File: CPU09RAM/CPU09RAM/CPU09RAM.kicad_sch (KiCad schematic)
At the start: 48 parts, among them J1 BUS, SW1 SW_DIP_x08, U1 74HC21, U10 AS6C4008-55PCN, U11 AS6C4008-55PCN, U12 74HC139, U13 74HC574, U14 74HC574, U15 74HC245, U16 74HC245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

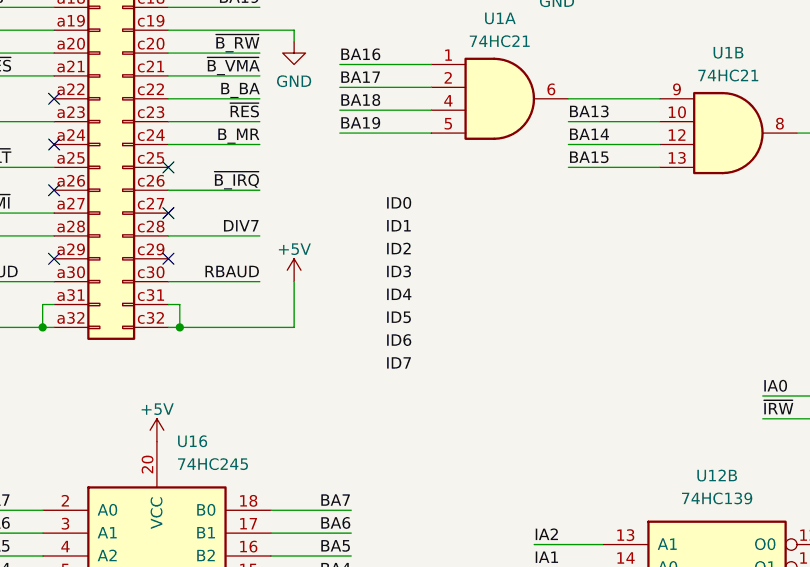
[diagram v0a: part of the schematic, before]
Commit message: 09NET added, 09FLP minor ch.
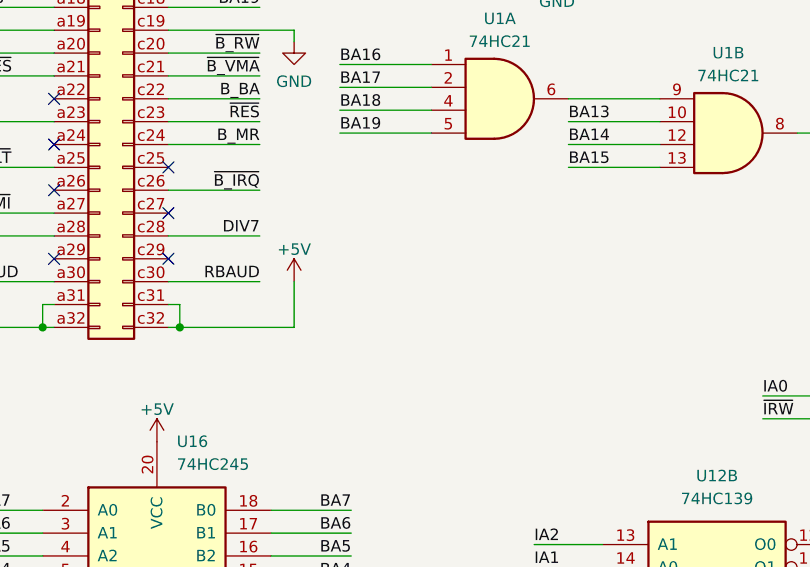
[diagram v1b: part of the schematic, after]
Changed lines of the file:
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@@
 		)
 	)
-	(label "ID2"
-		(at 67.31 92.71 0)
-		(effects
-			(font
-				(size 1.27 1.27)
-			)
-			(justify left bottom)
-		)
-	)
 	(label "LA8"
 		(at 113.03 173.99 180)
@@
 		)
 	)
-	(label "ID3"
-		(at 67.31 95.25 0)
-		(effects
-			(font
-				(size 1.27 1.27)
-			)
-			(justify left bottom)
-		)
-	)
 	(label "~{EXT}"
 		(at 53.34 29.21 180)
@@
 		)
 	)
-	(label "ID7"
-		(at 67.31 105.41 0)
-		(effects
-			(font
-				(size 1.27 1.27)
-			)
-			(justify left bottom)
-		)
-	)
 	(label "LA4"
 		(at 254 134.62 0)
@@
 		)
 	)
-	(label "ID1"
-		(at 67.31 90.17 0)
-		(effects
-			(font
-				(size 1.27 1.27)
-			)
-			(justify left bottom)
-		)
-	)
 	(label "IA3"
 		(at 254 39.37 0)
@@
 		)
 	)
-	(label "ID4"
-		(at 67.31 97.79 0)
-		(effects
-			(font
-				(size 1.27 1.27)
-			)
-			(justify left bottom)
-		)
-	)
-	(label "ID6"
-		(at 67.31 102.87 0)
-		(effects
-			(font
-				(size 1.27 1.27)
-			)
-			(justify left bottom)
-		)
-	)
 	(label "~{CE_U4}"
 		(at 303.53 181.61 180)
@@
 		)
 	)
-	(label "ID0"
-		(at 67.31 87.63 0)
-		(effects
-			(font
-				(size 1.27 1.27)
-			)
-			(justify left bottom)
-		)
-	)
 	(label "IA2"
 		(at 350.52 36.83 0)
@@
 		)
 	)
-	(label "ID5"
-		(at 67.31 100.33 0)
-		(effects
-			(font
-				(size 1.27 1.27)
-			)
-			(justify left bottom)
-		)
-	)
 	(label "LA1"
 		(at 205.74 57.15 0)
@@
 		(at 400.05 245.11 0)
 		(unit 1)
-		(exclude_from_sim no)
+		(exclude_from_sim yes)
 		(in_bom no)
 		(on_board no)
@@
 			(at 400.05 245.11 0)
 			(effects
-				(font
-					(size 1.27 1.27)
-				)
-				(hide yes)
-			)
-		)
-		(property "Sim.Enable" "0"
-			(at 400.05 245.11 0)
-			(effects

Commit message: new CPU09US4 Board added
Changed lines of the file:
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@@
 (kicad_sch
-	(version 20231120)
+	(version 20250114)
 	(generator "eeschema")
-	(generator_version "8.0")
+	(generator_version "9.0")
 	(paper "A3")
 	(title_block
@@
 		(comment 2 "v0.1:Initial")
 	)
+	(text "SW1-8,  ON = Format protection. Vdisk will not format.\nSW1-7,  ON = Reserve room for disk cache (SW1-4 must be OFF). \nSW1-6,  ON = Try for 2 virtual drives if SW1-3 or SW1-2 is ON. \nSW1-5,  ON = FLEX 512 byte pages, card present flag.\n\nSW1-4,  ON = FLEX 4MB disk\nSW1-3,  ON = FLEX 8\" DSDD\nSW1-2,  ON = FLEX 5\" DSDD\nSW1-1,  ON = Battery low set, Off = Sense Battery low "
+		(exclude_from_sim no)
+		(at 125.73 205.994 0)
+		(effects
+			(font
+				(size 1.27 1.27)
+			)
+			(justify left)
+		)
+	)
+	(text "G1\n"
+		(exclude_from_sim no)
+		(at 143.256 39.878 0)
+		(effects
+			(font
+				(size 1.27 1.27)
+			)
+		)
+	)
+	(text "X000-X1FF: RAM Access\nX200:  Latch L0...L7\nX201:  Latch L8...L11"
+		(exclude_from_sim no)
+		(at 39.116 269.748 0)
+		(effects
+			(font
+				(size 1.27 1.27)
+			)
+			(justify left)
+		)
+	)
 	(junction
 		(at 335.28 212.09)
@@
 		)
 	)
-	(text "SW1-8,  ON = Format protection. Vdisk will not format.\nSW1-7,  ON = Reserve room for disk cache (SW1-4 must be OFF). \nSW1-6,  ON = Try for 2 virtual drives if SW1-3 or SW1-2 is ON. \nSW1-5,  ON = FLEX 512 byte pages, card present flag.\n\nSW1-4,  ON = FLEX 4MB disk\nSW1-3,  ON = FLEX 8\" DSDD\nSW1-2,  ON = FLEX 5\" DSDD\nSW1-1,  ON = Battery low set, Off = Sense Battery low "
-		(exclude_from_sim no)
-		(at 125.73 205.994 0)
-		(effects
-			(font
-				(size 1.27 1.27)
-			)
-			(justify left)
-		)
-	)
-	(text "G1\n"
-		(exclude_from_sim no)
-		(at 143.256 39.878 0)
-		(effects
-			(font
-				(size 1.27 1.27)
-			)
-		)
-	)
-	(text "X000-X1FF: RAM Access\nX200:  Latch L0...L7\nX201:  Latch L8...L11"
-		(exclude_from_sim no)
-		(at 39.116 269.748 0)
-		(effects
-			(font
-				(size 1.27 1.27)
-			)
-			(justify left)
-		)
-	)
 	(label "ID0"
 		(at 251.46 101.6 180)
@@
 		)
 	)
+	(embedded_fonts no)
 )
